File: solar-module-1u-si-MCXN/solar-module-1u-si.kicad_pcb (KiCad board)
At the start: 2 copper layers, 83 x 100 mm, 143 parts, among them J1 MMS-104-01-[F/L]-SH, J2 2-1734592-0, Q1 NTR4101P, Q2 DMP2240UDM-7, U1 TCAN330, U10 TPS63060DSCR, U11 TMP101NA/3KSLOTTED, U12 LTC4412, U13 LTC4411, U14 LTC4411, U15 LTC4411, U16 LTC4411, U2 TMP101NA/3KSLOTTED, U3 LT1618EMSTRPBF, U4 INA226, U5 LTC4411, U6 LTC4411, U7 STM32F091CCT7, U8 LTC4411, U9 LTC4411, X1 ECS-160-10-36Q-ES-TR

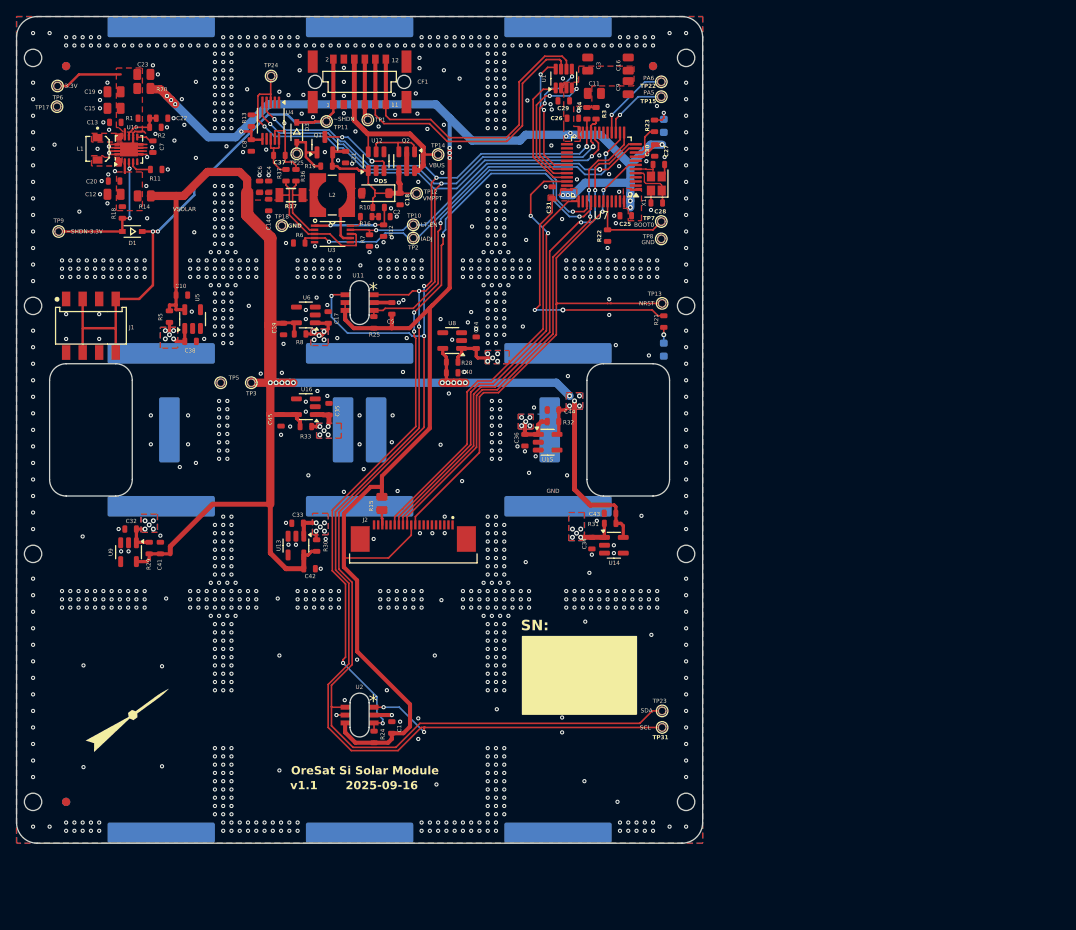
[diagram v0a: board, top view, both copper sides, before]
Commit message: moved to 4 layer board and added MCXN to PCB, some routing started
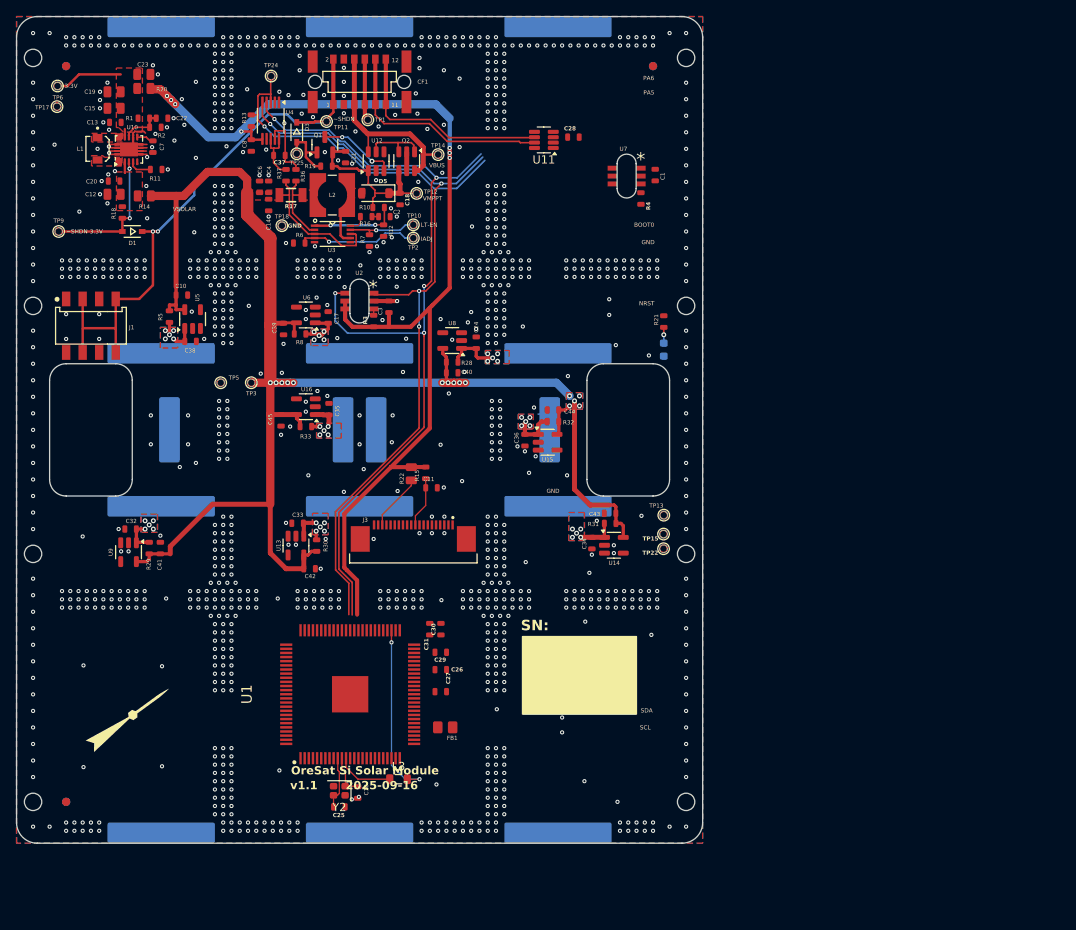
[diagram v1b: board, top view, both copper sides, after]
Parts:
- removed C5: 100n, oresat-passives:0603-C-NOSILK
- removed C9: 22u, oresat-passives:0805-C-NOSILK
- removed D6: AMBER, LED_SMD:LED_0603_1608Metric
- removed J2: 2-1734592-0, oresat-connectors:J-TE-2-1734592-0
- removed R23: 2.7k, oresat-passives:0603-C-NOSILK
- removed R24, R25: 10k, oresat-passives:0603-C-NOSILK
- removed TP23, TP31, TP7, TP8: TEST-POINT-LARGE-SQUARE, oresat-misc:TestPoint-0.75mm-th
- removed X1: ECS-160-10-36Q-ES-TR, oresat-misc:ECS-160-10-36Q-ES-TR
- added FB1: 120 ohm, oresat-passives:0805-B-NOSILK, F.Cu at (158.9, 141.0)
- added J3: OreSat Debug, oresat-connectors:J-TE-2-1734592-0, F.Cu at (155.0, 118.2)
- added L3: 1.5u, Inductor_SMD:L_0805_2012Metric, F.Cu at (153.2, 147.3)
- added Y2: 24 MHz, Crystal:Crystal_SMD_2016-4Pin_2.0x1.6mm, F.Cu at (146.1, 148.7)
- C11, C3: value 22u -> 100n; footprint oresat-passives:0805-C-NOSILK -> oresat-passives:0603-C-NOSILK
- C16: value 22u -> 4.7p; footprint oresat-passives:0805-C-NOSILK -> oresat-passives:0603-C-NOSILK
- C25: value 100n -> 4.7p
- C27: value 20p -> 4.7u
- C28: value 20p -> 100n
- C29: value 100n -> 6.8u
- C30: value 100n -> 4.7u
- C31: value 100n -> 2.2u
- R15: value 0 -> 10k; footprint oresat-passives:0805-C-NOSILK -> oresat-passives:0603-C-NOSILK
- R22: value 10k -> 0; footprint oresat-passives:0603-C-NOSILK -> oresat-passives:0805-C-NOSILK
- R3, R4: value 4.7k -> 10k
- TP13, TP15, TP22: value TEST-POINT-LARGE-SQUARE -> Test-Point
- U1: value TCAN330 -> MCXN947VKLT; footprint Package_TO_SOT_SMD:SOT-23-8 -> oresat-ics:MCXN947KVLT-QFP50P1600X1600X160-101N
- U11: value TMP101NA/3KSLOTTED -> TCAN330; footprint oresat-ics:DBV6-SLOT -> Package_TO_SOT_SMD:SOT-23-8
- U7: value STM32F091CCT7 -> TMP101NA/3KSLOTTED; footprint Package_QFP:LQFP-48_7x7mm_P0.5mm -> oresat-ics:DBV6-SLOT
- moved C16 94.0 mm to (148.3, 148.9), turned to -90 degrees
- moved C25 79.5 mm to (146.1, 150.6)
- moved U1 78.8 mm to (147.4, 137.0)
- moved C1 74.0 mm to (184.3, 74.2)
- moved C27 69.0 mm to (158.3, 136.7)
- moved C26 68.6 mm to (158.3, 134.0), turned to 0 degrees
- moved C29 68.3 mm to (158.3, 131.9)
- moved C30 63.4 mm to (158.3, 129.1)
- moved TP22 56.5 mm to (185.3, 119.4)
- moved C31 54.8 mm to (157.0, 129.1)
- moved TP15 52.9 mm to (185.3, 117.6)
- moved C11 51.6 mm to (157.2, 112.0)
- moved U2 50.1 mm to (148.5, 89.4)
- moved C3 38.0 mm to (152.1, 90.1)
- moved R22 37.3 mm to (154.8, 110.3), turned to 90 degrees
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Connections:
- C1 pad 1: 3.3V -> +3.3V
- C11 pad 1: 3.3V -> /Microcontroller/RESET
- C16 pad 1: 3.3V -> Net-(U1C-P1_31)
- C25 pad 1: GND -> Net-(U1C-P1_30)
- C25 pad 2: 3.3V -> GND
- C26 pad 1: GND -> VDD_CORE
- C26 pad 2: 3.3V -> GND
- C27 pad 1: /Microcontroller/OSC_OUT -> VDD_CORE
- C28 pad 1: /Microcontroller/OSC_IN -> +3.3V
- C29 pad 1: GND -> VDD_CORE
- C29 pad 2: 3.3V -> GND
- C3 pad 1: 3.3V -> +3.3V
- C30 pad 1: GND -> +3.3V
- C30 pad 2: 3.3V -> GND
- C31 pad 1: GND -> /Microcontroller/VDD_SYS
- C31 pad 2: 3.3V -> GND
- C8 pad 1: 3.3V -> +3.3V
- R13 pad 2: 3.3V -> +3.3V
- R15 pad 1: Net-(J2-DEBUG-1) -> /Microcontroller/RESET
- R15 pad 2: 3.3V -> +3.3V
- R20 pad 1: 3.3V -> +3.3V
- R21 pad 1: 3.3V -> +3.3V
- R22 pad 1: /Microcontroller/BOOT0 -> Net-(J3-DEBUG-1)
- R22 pad 2: GND -> +3.3V
- R3 pad 1: SCL -> Net-(U1F-P4_23)
- R3 pad 2: 3.3V -> +3.3V
- R4 pad 1: SDA -> Net-(U1F-P4_20)
- R4 pad 2: 3.3V -> +3.3V
- TP13 pad 1: /Microcontroller/NRESET -> ISP-UART_TXD
- TP15 pad 1: Net-(U7-PA5) -> ISP-UART_RXD
- TP22 pad 1: Net-(U7-PA6) -> /Microcontroller/VDD_ANA
- U1 pad 1: /Microcontroller/CAN_TX -> ISP-UART_RXD
- U1 pad 2: GND -> ISP-UART_TXD
- U1 pad 3: 3.3V -> Net-(U11-TXD)
- U1 pad 4: /Microcontroller/CAN_RX -> Net-(U11-RXD)
- U1 pad 5: /Microcontroller/CAN_SHDN -> unconnected-(U1C-P1_12-Pad5)
- U1 pad 6: CANL -> unconnected-(U1C-P1_13-Pad6)
- U1 pad 7: CANH -> unconnected-(U1C-P1_14-Pad7)
- U1 pad 8: /Microcontroller/CAN_SILENT -> unconnected-(U1C-P1_15-Pad8)
- U11 pad 1: SCL -> Net-(U11-TXD)
- U11 pad 3: Net-(U11-ALERT) -> +3.3V
- U11 pad 4: 3.3V -> Net-(U11-RXD)
- U11 pad 5: 3.3V -> Net-(U11-SHDN)
- U11 pad 6: SDA -> CANL
- U2 pad 3: Net-(U2-ALERT) -> Net-(U1F-P4_23)
- U2 pad 4: 3.3V -> +3.3V
- U2 pad 5: GND -> +3.3V
- U4 pad 6: 3.3V -> +3.3V
- U7 pad 1: 3.3V -> SCL
- U7 pad 2: unconnected-(U7-PC13-Pad2) -> GND
- U7 pad 3: unconnected-(U7-PC14-Pad3) -> Net-(U1F-P4_20)
- U7 pad 4: unconnected-(U7-PC15-Pad4) -> +3.3V
- U7 pad 5: /Microcontroller/OSC_IN -> GND
- U7 pad 6: /Microcontroller/OSC_OUT -> SDA
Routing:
- net 3.3V: track 247.1 -> 0.00 mm, vias 19 -> 0
- net +3.3V: track 0.00 -> 133.5 mm, vias 0 -> 7
- net Net-(U2-ALERT): track 96.4 -> 0.00 mm, vias 6 -> 0
- net SCL: track 180.2 -> 97.2 mm, vias 7 -> 4
- net SDA: track 182.0 -> 106.1 mm, vias 6 -> 5
- net /Microcontroller/NRESET: track 69.1 -> 0.00 mm, vias 2 -> 0
- net /Microcontroller/PA2/USART2_TX: track 60.8 -> 0.00 mm, vias 2 -> 0
- net /Microcontroller/PA3/USART2_RX: track 59.7 -> 0.00 mm, vias 2 -> 0
- net /Microcontroller/SWDIO: track 54.2 -> 0.00 mm, vias 2 -> 0
- net /Microcontroller/SWCLK: track 49.5 -> 0.00 mm
- net Net-(U11-ALERT): track 42.4 -> 0.00 mm, vias 2 -> 0
- net LT1618-IADJ: track 47.2 -> 14.6 mm, vias 2 -> 1
- net LT1618-ENABLE: track 40.3 -> 8.57 mm, vias 2 -> 1
- net Net-(U1A-DCDC_LX): track 0.00 -> 21.9 mm, vias 0 -> 2
- net /Microcontroller/CAN_RX: track 17.0 -> 0.00 mm, vias 2 -> 0
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- removed copper zone on F.Cu, net 3.3V
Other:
- copper layers 2 -> 4

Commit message: More routing work, pulled power routing onto another layer
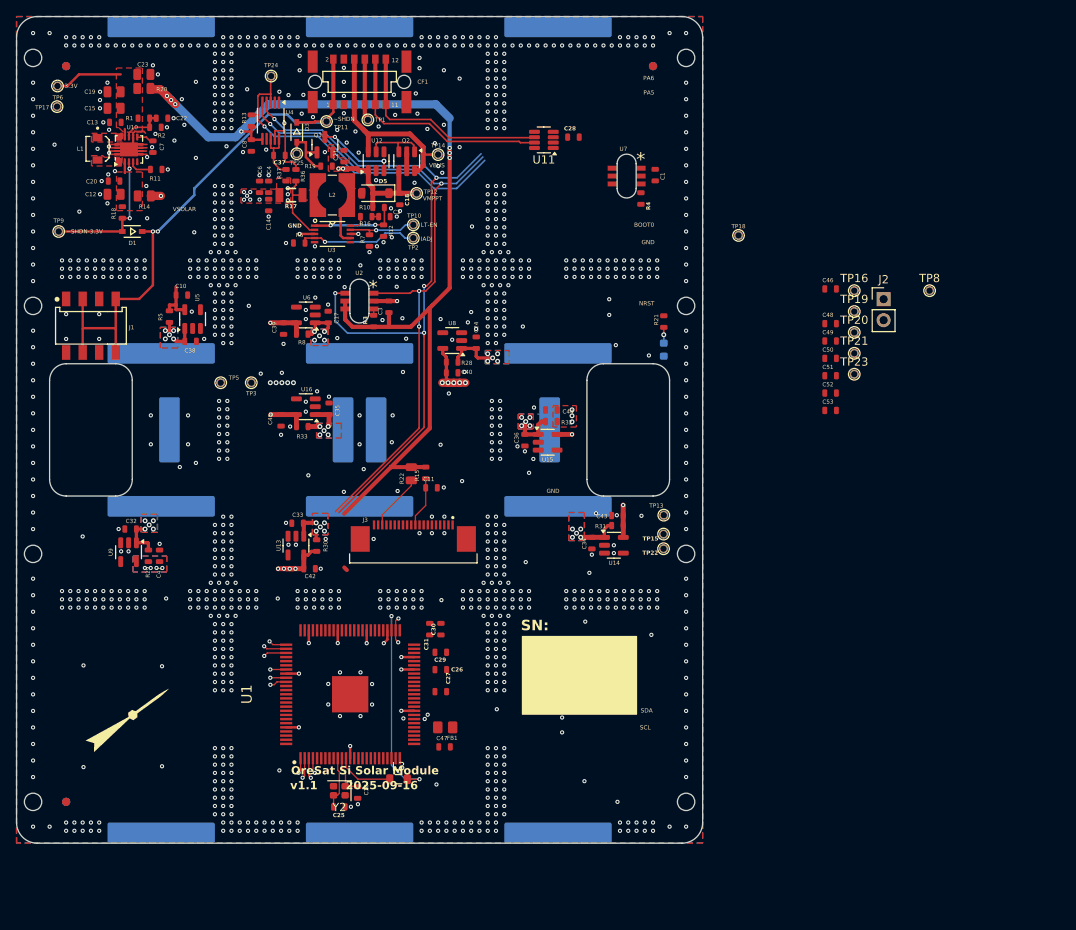
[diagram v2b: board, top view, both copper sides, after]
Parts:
- added C46: 100n, oresat-passives:0603-C-NOSILK, F.Cu at (205.5, 88.0)
- added C47: 1u, oresat-passives:0603-C-NOSILK, F.Cu at (158.8, 143.3)
- added C48: 100n, oresat-passives:0603-C-NOSILK, F.Cu at (205.5, 92.2)
- added C49: 100n, oresat-passives:0603-C-NOSILK, F.Cu at (205.5, 94.2)
- added C50: 100n, oresat-passives:0603-C-NOSILK, F.Cu at (205.5, 96.3)
- added C51: 100n, oresat-passives:0603-C-NOSILK, F.Cu at (205.5, 98.5)
- added C52: 100n, oresat-passives:0603-C-NOSILK, F.Cu at (205.5, 100.5)
- added C53: 100n, oresat-passives:0603-C-NOSILK, F.Cu at (205.5, 102.7)
- added J2: Conn_01x02, Connector_PinHeader_2.54mm:PinHeader_1x02_P2.54mm_Vertical, F.Cu at (211.9, 89.2)
- added TP16: Test-Point, oresat-misc:TestPoint-0.75mm-th, F.Cu at (208.3, 88.2)
- added TP19: Test-Point, oresat-misc:TestPoint-0.75mm-th, F.Cu at (208.3, 90.7)
- added TP20: Test-Point, oresat-misc:TestPoint-0.75mm-th, F.Cu at (208.3, 93.2)
- added TP21: Test-Point, oresat-misc:TestPoint-0.75mm-th, F.Cu at (208.3, 95.7)
- added TP23: Test-Point, oresat-misc:TestPoint-0.75mm-th, F.Cu at (208.3, 98.3)
- added TP8: TEST-POINT-LARGE-SQUARE, oresat-misc:TestPoint-0.75mm-th, F.Cu at (217.5, 88.2)
- moved TP18 55.3 mm to (194.3, 81.5)
- moved C41 0.95 mm to (124.3, 120.2)
- moved R29 0.95 mm to (123.0, 120.2)
- moved C43 0.93 mm to (179.7, 115.4)
- moved R31 0.92 mm to (179.7, 116.6)
- moved R33 0.43 mm to (141.6, 104.6)
- moved R8 0.26 mm to (141.6, 93.4)
- moved C21 0.21 mm to (146.6, 71.9), turned to 90 degrees
- moved C44 0.21 mm to (171.7, 102.6)
- moved R32 0.21 mm to (171.7, 104.0)
- moved C35 0.05 mm to (144.8, 102.5)
- moved C17 0.05 mm to (144.7, 91.3)
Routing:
- net +3.3V: track 133.5 -> 184.0 mm, vias 7 -> 17
- net SDA: track 106.1 -> 94.9 mm, vias 5 -> 6
- net SCL: track 97.2 -> 86.1 mm, vias 4 -> 5
- net /MPPT and Power/VMPPT: track 20.6 -> 16.4 mm, vias 0 -> 2
- net Net-(D7-A1): track 8.52 -> 4.79 mm
- net Net-(U1A-DCDC_LX): track 21.9 -> 25.3 mm
- net GND: track 13.2 -> 16.4 mm, vias 1118 -> 1133
- net /Microcontroller/SWO: track 0.00 -> 2.80 mm, vias 0 -> 1
- net /Microcontroller/SWCLK: track 0.00 -> 2.79 mm, vias 0 -> 1
- net Net-(U11-TXD): track 0.00 -> 2.46 mm, vias 0 -> 1
- net ISP-UART_TXD: track 0.00 -> 2.46 mm, vias 0 -> 1
- net /Microcontroller/SWDIO: track 0.00 -> 2.18 mm, vias 0 -> 1
- net Net-(J2-Pin_1): track 0.00 -> 1.92 mm, vias 0 -> 1
- net Net-(U11-RXD): track 0.00 -> 1.87 mm, vias 0 -> 1
- net ISP-UART_RXD: track 0.00 -> 1.86 mm, vias 0 -> 1
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- added copper zone on F.Cu, net /MPPT and Power/VMPPT
- added copper zone on In1.Cu, net GND
- added copper zone on In2.Cu, net VSOLAR

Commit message: more layout and routing
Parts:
- added R9: 10k, oresat-passives:0603-C-NOSILK, F.Cu at (136.2, 134.5)
- moved J2 109.7 mm to (112.0, 134.5)
- moved TP5 99.7 mm to (231.0, 89.8)
- moved TP24 98.7 mm to (231.0, 94.8), turned to 0 degrees
- moved TP3 95.6 mm to (231.0, 99.3)
- moved TP18 91.3 mm to (111.8, 120.5)
- moved TP23 53.8 mm to (185.3, 146.9)
- moved R4 47.8 mm to (226.1, 96.7), turned to 0 degrees
- moved U7 46.7 mm to (221.7, 96.7)
- moved C1 46.6 mm to (226.1, 94.6), turned to 0 degrees
- moved TP13 43.2 mm to (220.2, 89.8), turned to 0 degrees
- moved TP15 43.1 mm to (220.2, 92.3)
- moved TP22 21.4 mm to (185.3, 140.8)
- moved C29 17.6 mm to (150.5, 147.7), turned to -90 degrees
- moved TP20 17.2 mm to (225.2, 89.8)
- moved TP21 17.2 mm to (225.2, 92.3)
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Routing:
- net Net-(U11-RXD): track 1.87 -> 120.2 mm, vias 1 -> 2
- net Net-(U11-TXD): track 2.46 -> 112.5 mm, vias 1 -> 2
- net +3.3V: track 184.0 -> 98.2 mm, vias 17 -> 18
- net LT1618-ENABLE: track 8.57 -> 79.8 mm, vias 1 -> 2
- net LT1618-IADJ: track 14.6 -> 82.3 mm, vias 1 -> 2
- net INA226-nALERT: track 40.8 -> 102.3 mm, vias 1 -> 4
- net VDD_CORE: track 6.97 -> 63.1 mm
- net Net-(U1F-P4_23): track 0.77 -> 52.8 mm, vias 0 -> 2
- net /Microcontroller/RESET: track 6.12 -> 54.4 mm, vias 0 -> 2
- net ISP-UART_RXD: track 1.86 -> 38.3 mm, vias 1 -> 2
- net ISP-UART_TXD: track 2.46 -> 38.8 mm, vias 1 -> 2
- net /Microcontroller/VDD_ANA: track 0.00 -> 30.7 mm
- net Net-(J2-Pin_1): track 1.92 -> 32.4 mm, vias 1 -> 0
- net /Microcontroller/SWO: track 2.80 -> 26.2 mm, vias 1 -> 0
- net /Microcontroller/SWCLK: track 2.79 -> 25.5 mm, vias 1 -> 0
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- added copper zone on F.Cu, net +3.3V
- added copper zone on F.Cu, net VDD_CORE

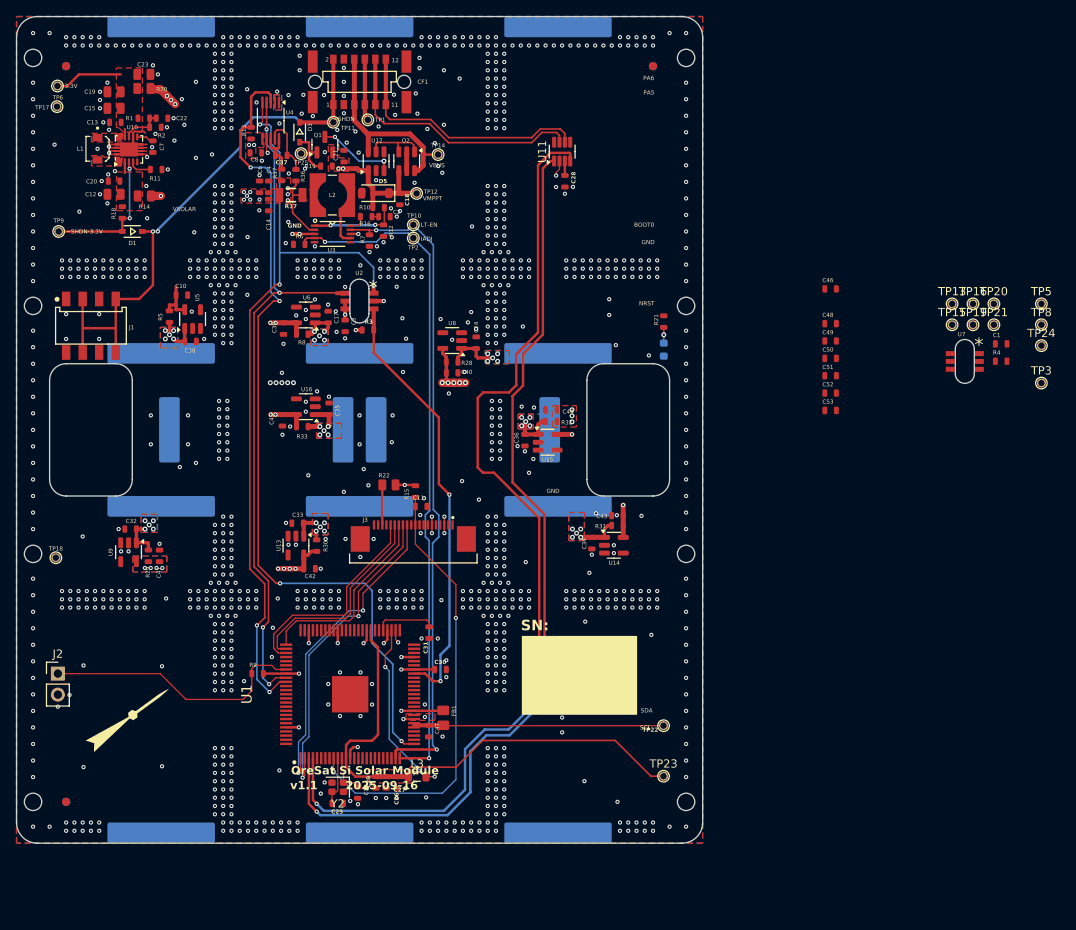
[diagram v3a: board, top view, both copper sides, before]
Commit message: Finished routing, starting on fixing DRC
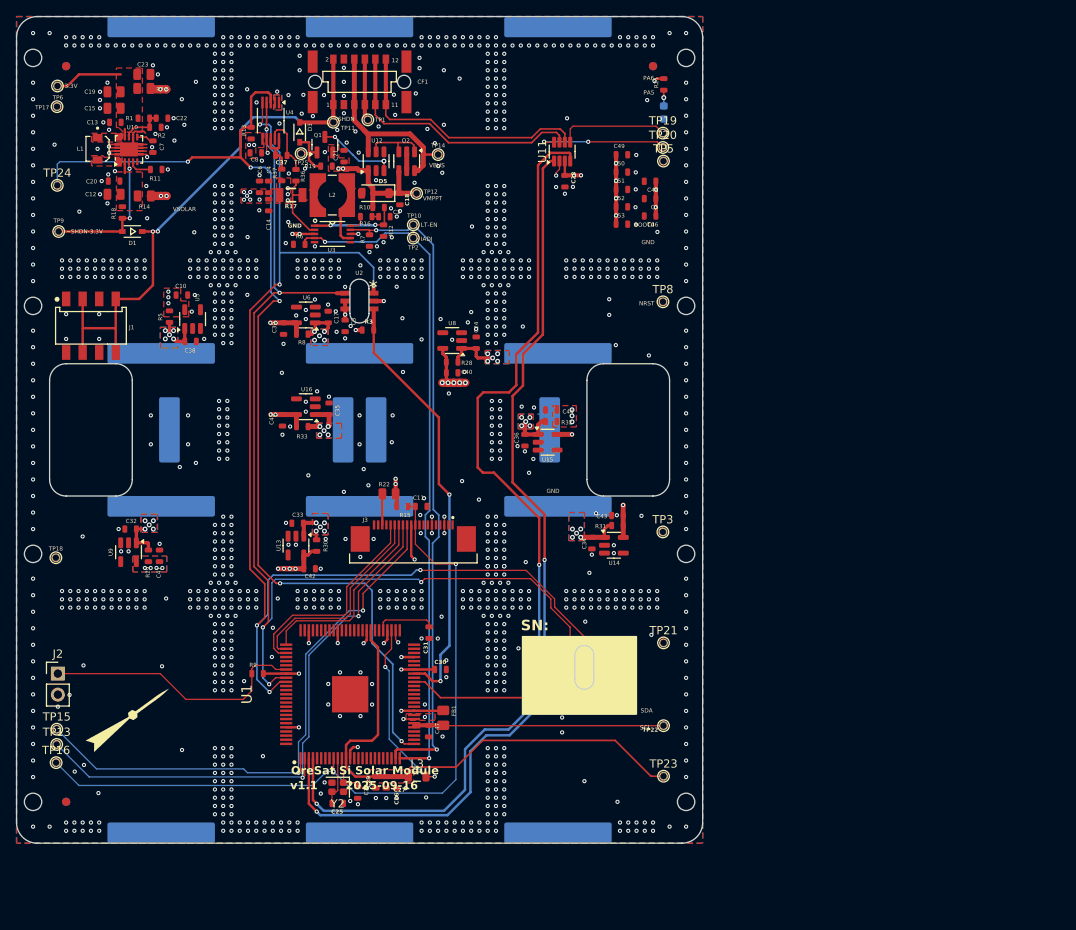
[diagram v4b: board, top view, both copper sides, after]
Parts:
- moved TP16 124.0 mm to (111.8, 145.3)
- moved TP13 120.7 mm to (111.9, 143.1)
- moved TP24 120.6 mm to (111.9, 75.4)
- moved TP15 118.8 mm to (111.9, 141.2)
- moved R4 62.0 mm to (178.1, 136.0)
- moved U7 59.1 mm to (175.7, 133.7)
- moved TP21 55.5 mm to (185.3, 130.8)
- moved TP3 49.2 mm to (185.2, 117.3)
- moved TP5 48.9 mm to (185.3, 72.5)
- moved C1 46.0 mm to (183.6, 77.0), turned to 180 degrees
- moved TP8 45.9 mm to (185.2, 89.5)
- moved TP20 44.3 mm to (185.2, 70.8)
- moved TP19 44.1 mm to (185.2, 69.1)
- moved C49 33.8 mm to (180.2, 71.7)
- moved C50 33.8 mm to (180.2, 73.8)
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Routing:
- net VSOLAR: track 204.7 -> 39.2 mm, vias 40 -> 39
- net SCL: track 94.4 -> 146.6 mm, vias 5 -> 6
- net SDA: track 84.3 -> 133.8 mm, vias 4 -> 5
- net /Microcontroller/RESET: track 54.4 -> 91.0 mm
- net ISP-UART_RXD: track 38.3 -> 69.7 mm
- net ISP-UART_TXD: track 38.8 -> 70.2 mm
- net Net-(U1F-P4_20): track 0.00 -> 25.4 mm
- net INA226-nALERT: track 102.3 -> 127.3 mm, vias 4 -> 5
- net +3.3V: track 98.2 -> 81.5 mm, vias 18 -> 31
- net Net-(U11-S): track 0.00 -> 15.9 mm, vias 0 -> 2
- net Net-(U11-SHDN): track 0.00 -> 13.3 mm
- net Net-(J3-DEBUG-1): track 4.84 -> 3.76 mm
- net GND: vias 1160 -> 1176
- added copper zone on In2.Cu, net +3.3V

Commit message: Fixed most DRC errors
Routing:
- net GND: track 22.1 -> 24.7 mm, vias 1176 -> 1174
- net +3.3V: track 81.5 -> 82.3 mm
- net Net-(D9-A1): track 5.71 -> 5.00 mm
- net SDA: vias 5 -> 7
- net SCL: vias 6 -> 8
- net Net-(D11-A1): vias 6 -> 5
- net /MPPT and Power/VMPPT: vias 2 -> 0
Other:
- board text added: "make sure to update version and date on silkscreen"
